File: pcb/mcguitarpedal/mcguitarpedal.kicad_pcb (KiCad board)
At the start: 2 copper layers, 132 x 123 mm, 65 parts, among them J1 IN, J10 ENCODER2, J11 ENCODER3, J2 PREAMP_HEADERS, J3 BTN_MTX, J4 OUT, J5 EXP, J6 ILI9488 Module, J7 PWR_IN, J8 POT_HP_VOLUME_10k, J9 ENCODER1, SW1 SW_BYPASS, SW2 SW_TUNER, SW3 SW_PRESET, SW4 LINE_LEVEL, U1 Teensy4.0_AudioShield_REVD, U2 Teensy4.1, U3 LM4562, U4 74HC148, U5 74HC4094, U6 STPDWN-3P-5V, U7 STDN-3A24-ADJ

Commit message: Changed to DPDT switches
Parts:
- removed JP1: JP_SIGNAL_PREAMP, Connector_PinHeader_2.54mm:PinHeader_1x02_P2.54mm_Vertical
- removed SW2: SW_TUNER, TI_FOOTPRINTS:01-690DB_3PDT_JCV_OVAL
- removed U1: Teensy4.0_AudioShield_REVD, teensy_audio_shield:4.0audioshield_reference
- added C8: 100nf, Capacitor_THT:C_Rect_L7.2mm_W2.5mm_P5.00mm_FKS2_FKP2_MKS2_MKP2, F.Cu at (73.3, 59.0)
- added D10: D_Schottky, TI_FOOTPRINTS:DO-41_DIO, F.Cu at (89.8, 80.5)
- added D9: D_Schottky, TI_FOOTPRINTS:DO-41_DIO, F.Cu at (101.0, 77.3)
- added JP5: JP_SW1_LED, Connector_PinHeader_2.54mm:PinHeader_1x03_P2.54mm_Vertical, F.Cu at (75.8, 132.5)
- added JP6: JP_SW1_LED, Connector_PinHeader_2.54mm:PinHeader_1x03_P2.54mm_Vertical, F.Cu at (108.2, 132.5)
- added POT1: Logo_Open_Hardware_Small, mcguitarpedal:Floating Potentiometer, F.Cu at (162.0, 38.0)
- added POT2: Logo_Open_Hardware_Small, mcguitarpedal:Floating Potentiometer, F.Cu at (162.0, 78.0)
- added POT3: Logo_Open_Hardware_Small, mcguitarpedal:Floating Potentiometer, F.Cu at (162.0, 58.0)
- added R24: 500, Resistor_THT:R_Axial_DIN0207_L6.3mm_D2.5mm_P7.62mm_Horizontal, F.Cu at (89.8, 83.4)
- added SW5: SW_TUNER, mcguitarpedal:SW_PUSH_DPDT, F.Cu at (90.4, 127.4)
- added SW6: SW_PRESET, mcguitarpedal:SW_PUSH_DPDT, F.Cu at (122.9, 127.4)
- C1, C3, C7: footprint Capacitor_THT:C_Rect_L18.0mm_W5.0mm_P15.00mm_FKS3_FKP3 -> Capacitor_THT:C_Rect_L7.2mm_W3.5mm_P5.00mm_FKS2_FKP2_MKS2_MKP2
- SW1: footprint TI_FOOTPRINTS:01-690DB_3PDT_JCV_OVAL -> mcguitarpedal:SW_PUSH_DPDT
- U2: footprint mcguitarpedal:PinHeader_2x24_P2.54mm_W15.24_Vertical -> mcguitarpedal:Teensy 4.1 with audio board
- moved SW3 159.0 mm to (259.7, 213.6)
- moved R7 69.7 mm to (37.7, 43.3), turned to 0 degrees
- moved C4 68.4 mm to (18.2, 36.5)
- moved R9 67.8 mm to (16.9, 41.1)
- moved R17 57.8 mm to (137.2, 50.8), turned to -90 degrees
- moved C6 56.1 mm to (39.2, 36.5)
- moved R6 54.8 mm to (49.4, 42.5), turned to -90 degrees
- moved R5 54.3 mm to (37.4, 47.1)
- moved R10 54.2 mm to (37.3, 51.2)
- moved C5 54.1 mm to (32.4, 43.4)
- moved R8 54.1 mm to (33.8, 36.5)
- moved JP3 53.4 mm to (134.1, 49.5), turned to 0 degrees
- moved J2 52.5 mm to (99.9, 88.8), turned to -90 degrees
- moved R11 42.3 mm to (80.0, 79.4), turned to 0 degrees
- moved R12 36.5 mm to (87.6, 74.2), turned to 180 degrees
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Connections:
- net Net-(J4-PadT) renamed /SIGNAL_OUT
- net Net-(J8A-Pin_1) renamed /preamp/STAGE1_FEEDBACK
- net Net-(U3B--) renamed /preamp/STAGE2_OUT
- J2 pad 6: /preamp/PREAMP_OUT -> /LINE_IN
- R11 pad 1: 3.3V -> TEENSY_3.3V
- R13 pad 2: 3.3V -> Net-(JP5-C)
- R14 pad 2: 3.3V -> Net-(JP6-C)
- SW1 pad 4: /SIGNAL_IN -> 3.3V
- SW1 pad 5: /PREAMP_IN -> /1_SW1
- SW4 pad 1: /PREAMP_IN -> /SIGNAL_IN
- SW4 pad 2: /PREAMP_IN -> /SIGNAL_IN
- SW4 pad 6: /PREAMP_IN -> /SIGNAL_IN
- U2 pad 15: unconnected-(U2-3V3-Pad15) -> TEENSY_3.3V
- U2 pad 46: unconnected-(U2-3V3-Pad46) -> TEENSY_3.3V
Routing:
- net /PREAMP_IN: track 211.4 -> 0.00 mm, vias 4 -> 0
- net /A3_EXP: track 84.7 -> 11.3 mm, vias 2 -> 0
- net Net-(J6-SDO(MISO)): track 84.0 -> 14.7 mm
- net /39_TFT_MISO: track 6.50 -> 69.4 mm
- net 3.3V: track 402.4 -> 349.3 mm
- net /A1_VOLUME: track 104.4 -> 60.2 mm
- net /SIGNAL_IN: track 204.0 -> 169.3 mm, vias 4 -> 2
- net Net-(U3B-+): track 32.0 -> 0.00 mm
- net /LED_STR: track 75.3 -> 45.9 mm, vias 4 -> 2
- net Net-(C4-Pad1): track 21.3 -> 0.00 mm
- net /preamp/STAGE1_IN: track 96.6 -> 78.7 mm, vias 1 -> 3
- net /preamp/PREAMP_OUT: track 0.00 -> 16.4 mm
- net Net-(C6-Pad2): track 15.2 -> 0.00 mm
- net /preamp/STAGE1_OUT: track 129.7 -> 115.1 mm
- net /preamp/STAGE1_FEEDBACK: track 72.1 -> 82.5 mm
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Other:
- board size 132 x 123 mm -> 129.5 x 123 mm
- board text added: "TODO: Audio board 3V3 PWR LEDs Testpoints Encoders Evenly distribute jacks Mounting holes Footswitch pushbutton Switch 470n to smaller footprint Move 5V regulator above U5"
- board text removed: "TODO: Audio board 3V3 PWR LEDs Testpoints Encoders Evenly distribute jacks Mounting holes Footswitch pushbutton Switch 470n to smaller footprint"

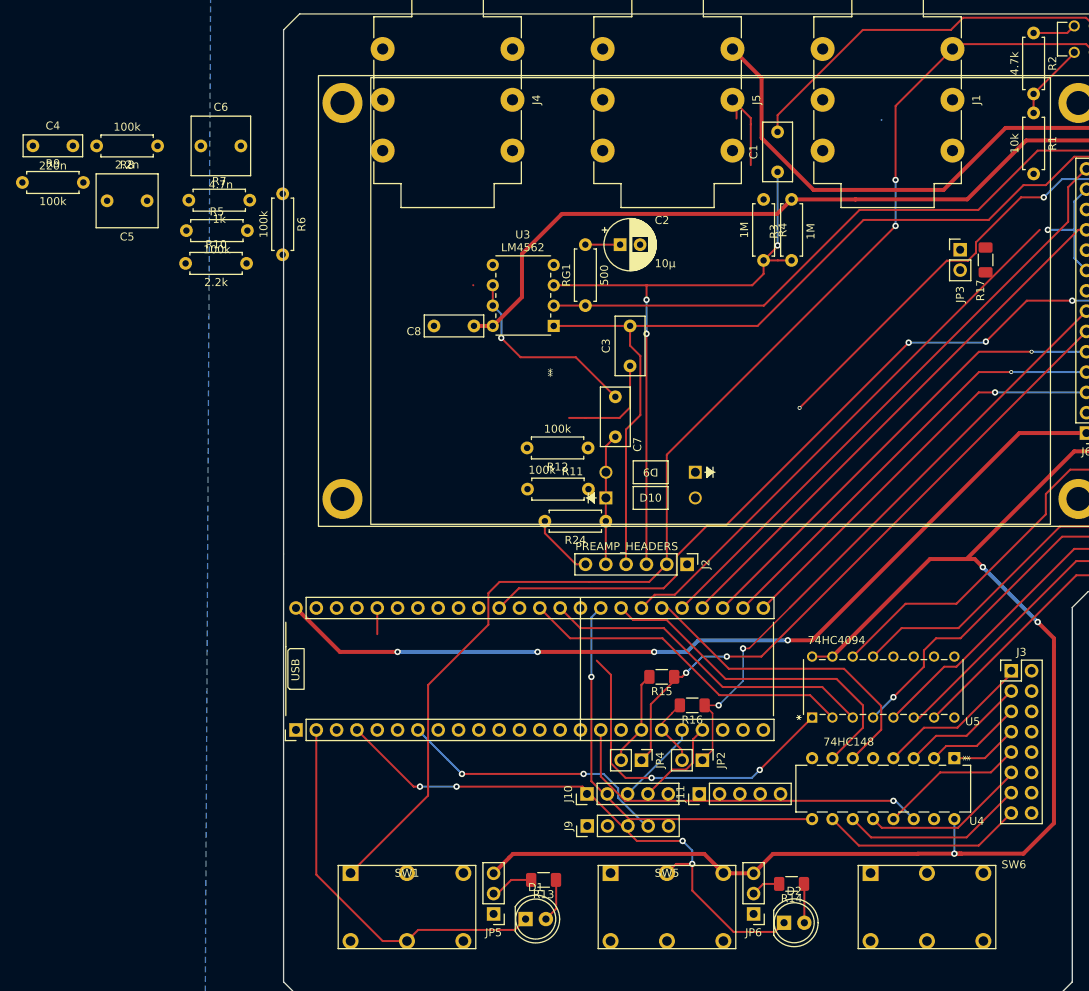
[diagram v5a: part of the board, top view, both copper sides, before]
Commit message: Rearranged preamp circuit
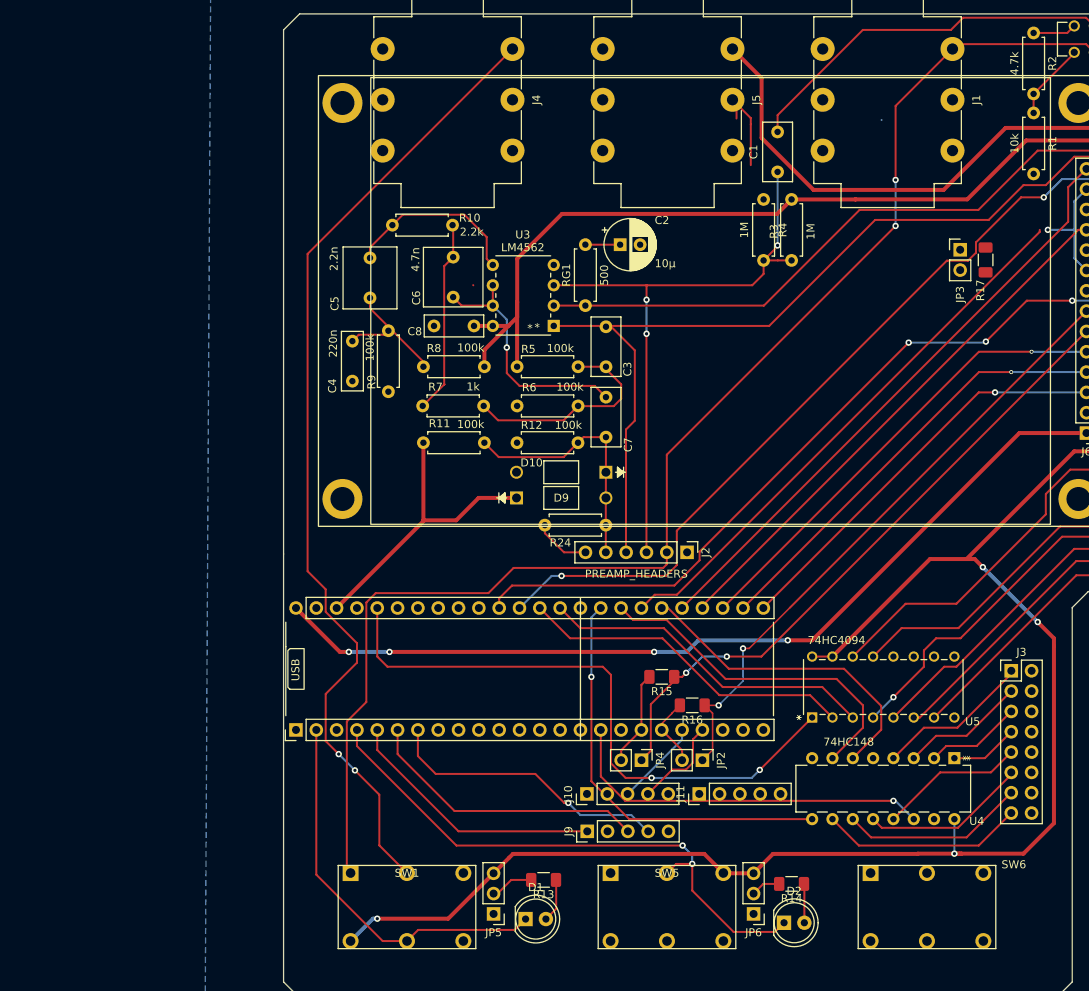
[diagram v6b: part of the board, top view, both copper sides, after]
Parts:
- moved R9 49.4 mm to (62.6, 59.6), turned to -90 degrees
- moved R8 49.3 mm to (74.6, 64.1)
- moved C4 46.8 mm to (58.1, 60.9), turned to -90 degrees
- moved R6 45.5 mm to (86.3, 69.0), turned to 180 degrees
- moved R5 44.7 mm to (78.7, 64.1)
- moved R7 38.9 mm to (66.9, 69.0)
- moved C6 36.8 mm to (70.7, 55.4), turned to 90 degrees
- moved C5 28.8 mm to (60.3, 50.5), turned to -90 degrees
- moved R10 26.2 mm to (63.0, 46.4)
- moved D9 22.6 mm to (78.6, 80.5), turned to 0 degrees
- moved R11 14.2 mm to (67.0, 73.6)
- moved D10 3.21 mm to (89.8, 77.3), turned to 180 degrees
- moved C3 3.01 mm to (89.8, 64.1)
- moved J2 1.50 mm to (99.9, 87.3)
- moved R12 1.42 mm to (86.3, 73.6)
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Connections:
- D9 pad 1: 3.3V -> TEENSY_3.3V
- U2 pad 15: TEENSY_3.3V -> unconnected-(U2-3V3-Pad15)
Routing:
- net /SIGNAL_OUT: track 0.00 -> 122.0 mm, vias 0 -> 2
- net /A1_VOLUME: track 60.2 -> 108.1 mm
- net TEENSY_3.3V: track 0.00 -> 38.0 mm
- net /4_ENC_1_L: track 0.00 -> 35.8 mm
- net /3_ENC_1_BTN: track 0.00 -> 33.0 mm
- net /LED_STR: track 45.9 -> 76.3 mm
- net Net-(C6-Pad2): track 0.00 -> 24.2 mm
- net Net-(U3B-+): track 0.00 -> 22.5 mm
- net 3.3V: track 349.3 -> 370.7 mm, vias 5 -> 6
- net Net-(C4-Pad1): track 0.00 -> 16.7 mm
- net 9V: track 123.4 -> 138.5 mm
- net /preamp/PREAMP_OUT: track 16.4 -> 31.4 mm
- net /preamp/STAGE2_IN: track 13.4 -> 27.4 mm
- net /SIGNAL_IN: track 169.3 -> 178.0 mm
- net /preamp/STAGE2_OUT: track 24.4 -> 30.7 mm
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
